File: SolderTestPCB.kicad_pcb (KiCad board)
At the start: 2 copper layers, 2 parts, among them U1 L78L33_TO92, U3 ESP-12F

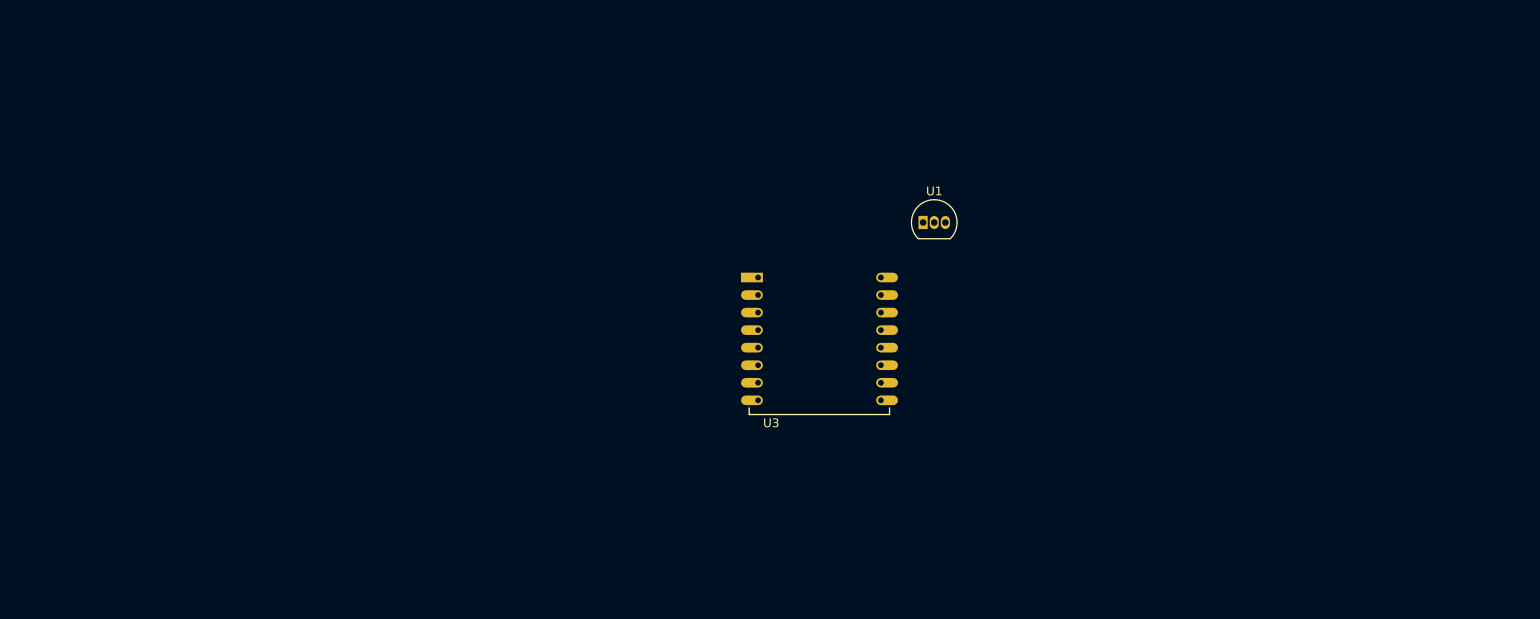
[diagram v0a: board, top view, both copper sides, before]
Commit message: Schematic ready; PCB needs silkscreen
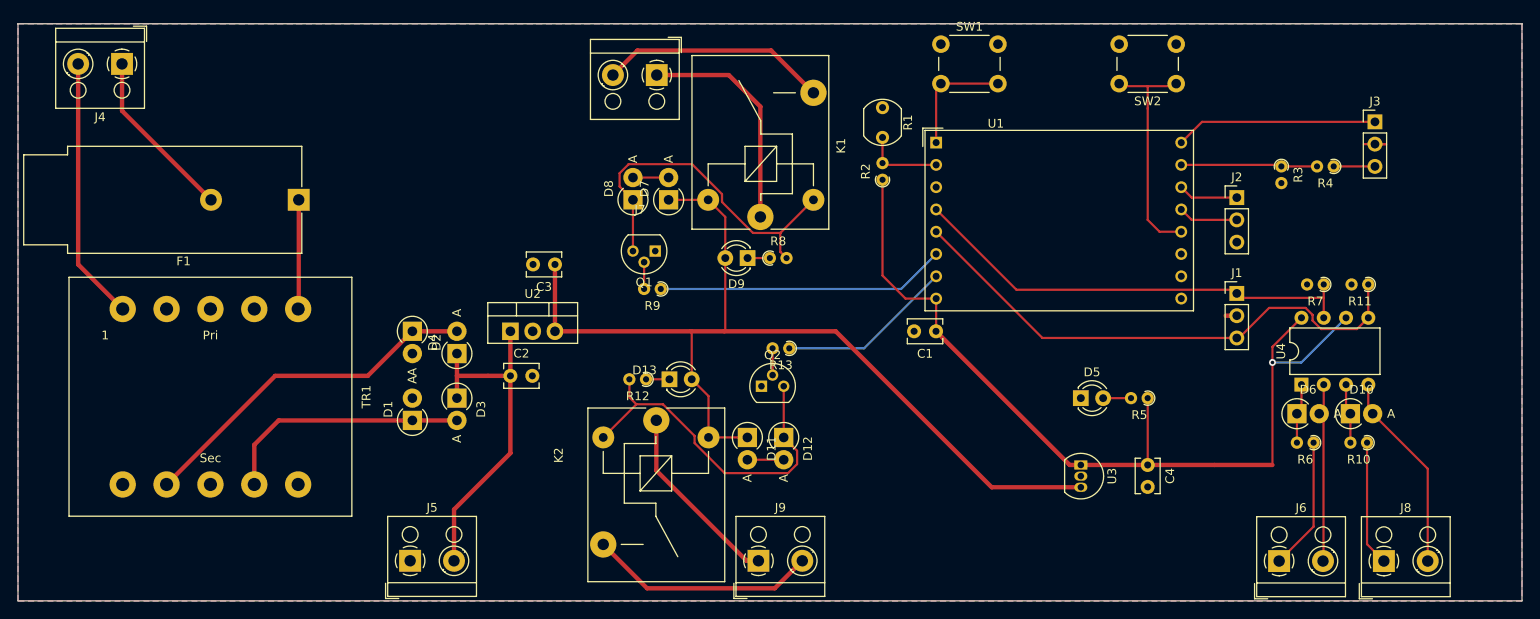
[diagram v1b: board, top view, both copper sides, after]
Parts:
- added C1: 100nF, Capacitor_THT:C_Disc_D3.8mm_W2.6mm_P2.50mm, F.Cu at (170.2, 103.6)
- added C2: C, Capacitor_THT:C_Disc_D3.8mm_W2.6mm_P2.50mm, F.Cu at (121.7, 108.7)
- added C3: C, Capacitor_THT:C_Disc_D3.8mm_W2.6mm_P2.50mm, F.Cu at (126.7, 96.0)
- added C4: C, Capacitor_THT:C_Disc_D3.8mm_W2.6mm_P2.50mm, F.Cu at (194.3, 118.9)
- added D1: D_45deg, Diode_THT:D_DO-41_SOD81_P2.54mm_Vertical_AnodeUp, F.Cu at (110.5, 113.8)
- added D10: D, Diode_THT:D_DO-41_SOD81_P2.54mm_Vertical_AnodeUp, F.Cu at (217.4, 113.0)
- added D11: D, Diode_THT:D_DO-41_SOD81_P2.54mm_Vertical_AnodeUp, F.Cu at (148.7, 115.7)
- added D12: D_Zener, Diode_THT:D_DO-41_SOD81_P2.54mm_Vertical_AnodeUp, F.Cu at (152.8, 115.7)
- added D13: LED, LED_THT:LED_D3.0mm, F.Cu at (139.8, 109.1)
- added D2: D_45deg, Diode_THT:D_DO-41_SOD81_P2.54mm_Vertical_AnodeUp, F.Cu at (110.5, 103.6)
- added D3: D_45deg, Diode_THT:D_DO-41_SOD81_P2.54mm_Vertical_AnodeUp, F.Cu at (115.6, 111.3)
- added D4: D_45deg, Diode_THT:D_DO-41_SOD81_P2.54mm_Vertical_AnodeUp, F.Cu at (115.6, 106.2)
- added D5: LED, LED_THT:LED_D3.0mm, F.Cu at (186.7, 111.3)
- added D6: D, Diode_THT:D_DO-41_SOD81_P2.54mm_Vertical_AnodeUp, F.Cu at (211.3, 113.0)
- added D7: D, Diode_THT:D_DO-41_SOD81_P2.54mm_Vertical_AnodeUp, F.Cu at (139.7, 88.6)
- added D8: D_Zener, Diode_THT:D_DO-41_SOD81_P2.54mm_Vertical_AnodeUp, F.Cu at (135.6, 88.6)
- added D9: LED, LED_THT:LED_D3.0mm, F.Cu at (148.7, 95.3)
- added F1: Fuse, Fuse:Fuseholder_Cylinder-5x20mm_Schurter_FAB_0031-355x_Horizontal_Closed, F.Cu at (97.5, 88.6)
- added J1: CON_INPUT, Connector_PinHeader_2.54mm:PinHeader_1x03_P2.54mm_Vertical, F.Cu at (204.5, 99.3)
- added J2: CON_I2C, Connector_PinHeader_2.54mm:PinHeader_1x03_P2.54mm_Vertical, F.Cu at (204.5, 88.4)
- added J3: CON_SERIAL, Connector_PinHeader_2.54mm:PinHeader_1x03_P2.54mm_Vertical, F.Cu at (220.2, 79.8)
- added J4: Screw_Terminal_01x02, TerminalBlock_RND:TerminalBlock_RND_205-00001_1x02_P5.00mm_Horizontal, F.Cu at (77.4, 73.2)
- added J5: Screw_Terminal_01x02, TerminalBlock_RND:TerminalBlock_RND_205-00001_1x02_P5.00mm_Horizontal, F.Cu at (110.2, 129.8)
- added J6: Screw_Terminal_01x02, TerminalBlock_RND:TerminalBlock_RND_205-00001_1x02_P5.00mm_Horizontal, F.Cu at (209.3, 129.8)
- added J7: Screw_Terminal_01x02, TerminalBlock_RND:TerminalBlock_RND_205-00001_1x02_P5.00mm_Horizontal, F.Cu at (138.3, 74.4)
- added J8: Screw_Terminal_01x02, TerminalBlock_RND:TerminalBlock_RND_205-00001_1x02_P5.00mm_Horizontal, F.Cu at (221.2, 129.8)
- added J9: Screw_Terminal_01x02, TerminalBlock_RND:TerminalBlock_RND_205-00001_1x02_P5.00mm_Horizontal, F.Cu at (149.9, 129.8)
- added K1: Relay_SPST-NO, Relay_THT:Relay_SPST_SANYOU_SRD_Series_Form_A, F.Cu at (150.2, 90.6)
- added K2: Relay_SPST-NO, Relay_THT:Relay_SPST_SANYOU_SRD_Series_Form_A, F.Cu at (138.3, 113.8)
- added Q1: Q_NPN_EBC, Package_TO_SOT_THT:TO-92, F.Cu at (138.2, 94.5)
- added Q2: Q_NPN_EBC, Package_TO_SOT_THT:TO-92, F.Cu at (150.3, 109.9)
- added R1: R_Photo, OptoDevice:R_LDR_5.1x4.3mm_P3.4mm_Vertical, F.Cu at (164.1, 78.1)
- added R10: R, Resistor_THT:R_Axial_DIN0204_L3.6mm_D1.6mm_P1.90mm_Vertical, F.Cu at (219.3, 116.3)
- added R11: R, Resistor_THT:R_Axial_DIN0204_L3.6mm_D1.6mm_P1.90mm_Vertical, F.Cu at (219.5, 98.3)
- added R12: R, Resistor_THT:R_Axial_DIN0204_L3.6mm_D1.6mm_P1.90mm_Vertical, F.Cu at (137.1, 109.1)
- added R13: R, Resistor_THT:R_Axial_DIN0204_L3.6mm_D1.6mm_P1.90mm_Vertical, F.Cu at (153.5, 105.6)
- added R2: R, Resistor_THT:R_Axial_DIN0204_L3.6mm_D1.6mm_P1.90mm_Vertical, F.Cu at (164.1, 86.4)
- added R3: R, Resistor_THT:R_Axial_DIN0204_L3.6mm_D1.6mm_P1.90mm_Vertical, F.Cu at (209.6, 84.8)
- added R4: R, Resistor_THT:R_Axial_DIN0204_L3.6mm_D1.6mm_P1.90mm_Vertical, F.Cu at (215.5, 84.8)
- added R5: R, Resistor_THT:R_Axial_DIN0204_L3.6mm_D1.6mm_P1.90mm_Vertical, F.Cu at (194.3, 111.3)
- added R6: R, Resistor_THT:R_Axial_DIN0204_L3.6mm_D1.6mm_P1.90mm_Vertical, F.Cu at (213.2, 116.3)
- added R7: R, Resistor_THT:R_Axial_DIN0204_L3.6mm_D1.6mm_P1.90mm_Vertical, F.Cu at (214.4, 98.3)
- added R8: R, Resistor_THT:R_Axial_DIN0204_L3.6mm_D1.6mm_P1.90mm_Vertical, F.Cu at (151.2, 95.3)
- added R9: R, Resistor_THT:R_Axial_DIN0204_L3.6mm_D1.6mm_P1.90mm_Vertical, F.Cu at (138.8, 98.8)
- added SW1: SW_RST, Button_Switch_THT:SW_PUSH_6mm_H4.3mm, F.Cu at (170.7, 70.9)
- added SW2: SW_PRG, Button_Switch_THT:SW_PUSH_6mm_H4.3mm, F.Cu at (197.6, 75.4)
- added TR1: TRANSF1, Transformer_THT:Transformer_CHK_EI30-2VA_1xSec, F.Cu at (77.5, 101.1)
- added U2: L7805, Package_TO_SOT_THT:TO-220-3_Vertical, F.Cu at (121.7, 103.6)
- added U4: LTV-827, Package_DIP:DIP-8_W7.62mm, F.Cu at (211.8, 109.7)
- U1: value L78L33_TO92 -> ESP-12; footprint Package_TO_SOT_THT:TO-92_Inline -> RF_Module:HOPERF_RFM9XW_THT
- U3: value ESP-12F -> L78L33_TO92; footprint ESP8266:ESP-12 -> Package_TO_SOT_THT:TO-92_Inline
- moved U3 42.5 mm to (186.7, 118.9), turned to -90 degrees
- moved U1 9.23 mm to (170.2, 82.1)
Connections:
- U1 pad 2: unconnected-(U1-GND-Pad2) -> Net-(U1-ADC)
- U1 pad 3: Net-(U1-VI) -> unconnected-(U1-CH_PD-Pad3)
- U3 pad 1: unconnected-(U3-REST-Pad1) -> VCC
- U3 pad 2: unconnected-(U3-ADC-Pad2) -> GND
- U3 pad 3: unconnected-(U3-CH_PD-Pad3) -> +5V
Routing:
- net +5V: track 0.00 -> 112.6 mm
- net VCC: track 0.00 -> 102.8 mm, vias 0 -> 1
- net Net-(J1-Pin_3): track 0.00 -> 61.4 mm
- net Net-(J1-Pin_1): track 0.00 -> 52.4 mm
- net Net-(D2-K): track 0.00 -> 40.7 mm
- net Net-(D8-K): track 0.00 -> 40.5 mm
- net Net-(D12-K): track 0.00 -> 40.5 mm
- net Net-(D3-K): track 0.00 -> 40.0 mm
- net /Output0/Control: track 0.00 -> 33.1 mm
- net Net-(J4-Pin_2): track 0.00 -> 30.0 mm
- net Net-(D1-K): track 0.00 -> 28.9 mm
- net Net-(U1-GPIO0): track 0.00 -> 26.1 mm
- net Net-(J9-Pin_2): track 0.00 -> 26.1 mm
- net Net-(J7-Pin_2): track 0.00 -> 26.0 mm
- net Net-(J7-Pin_1): track 0.00 -> 25.9 mm
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- added copper zone on B.Cu, net GND
- added copper zone on F.Cu, net GND
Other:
- board outline added: 171.4 x 65.8 mm

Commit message: PCB Layout finished (RTM)
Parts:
- added H1: MountingHole, MountingHole:MountingHole_3.2mm_M3, F.Cu at (70.1, 129.8)
- added H2: MountingHole, MountingHole:MountingHole_3.2mm_M3, F.Cu at (70.1, 73.2)
- added H3: MountingHole, MountingHole:MountingHole_3.2mm_M3, F.Cu at (190.8, 73.2)
- added H4: MountingHole, MountingHole:MountingHole_3.2mm_M3, F.Cu at (190.8, 129.8)
- added H5: MountingHole, MountingHole:MountingHole_2.7mm_M2.5, F.Cu at (80.0, 73.2)
- added H6: MountingHole, MountingHole:MountingHole_2.7mm_M2.5, F.Cu at (104.4, 73.2)
- added H7: MountingHole, MountingHole:MountingHole_2.7mm_M2.5, F.Cu at (80.0, 129.8)
- added H8: MountingHole, MountingHole:MountingHole_2.7mm_M2.5, F.Cu at (104.4, 129.8)
- AC IN: renamed from J4
- C2, C3: footprint Capacitor_THT:C_Disc_D3.8mm_W2.6mm_P2.50mm -> Capacitor_THT:C_Radial_D10.0mm_H12.5mm_P5.00mm
- C4: footprint Capacitor_THT:C_Disc_D3.8mm_W2.6mm_P2.50mm -> Capacitor_THT:C_Radial_D6.3mm_H7.0mm_P2.50mm
- D1, D10, D11, D12, D2, D3, D4, D6, D7, D8: footprint Diode_THT:D_DO-41_SOD81_P2.54mm_Vertical_AnodeUp -> Diode_THT:D_DO-15_P10.16mm_Horizontal
- DC IN: renamed from J5
- Light Sensor: renamed from R1
- moved D6 52.2 mm to (159.5, 119.1)
- moved R6 52.1 mm to (161.5, 122.7)
- moved R11 48.2 mm to (171.7, 105.2)
- moved R7 48.2 mm to (166.6, 105.2)
- moved U4 48.1 mm to (164.1, 115.6)
- moved IN1 47.7 mm to (161.6, 129.8)
- moved IN2 47.7 mm to (173.5, 129.8)
- moved R10 46.3 mm to (173.5, 122.7), turned to 0 degrees
- moved D10 44.6 mm to (173.2, 119.1)
- moved C4 44.0 mm to (153.7, 102.1), turned to 0 degrees
- moved R4 42.0 mm to (176.8, 101.1)
- moved R3 39.6 mm to (174.9, 103.9), turned to 0 degrees
- moved SW_RST 39.0 mm to (180.4, 108.7)
- moved INs 38.6 mm to (165.9, 101.1), turned to 90 degrees
- moved R5 36.2 mm to (158.2, 108.0), turned to -90 degrees
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- renumbered D5 to 3.3V, U1 to ESP8266_ADAPTER, J2 to I2C, J6 to IN1, J8 to IN2, J1 to INs, D9 to OUT1, J7 to OUT1, J9 to OUT2, D13 to OUT2, J3 to SERIAL, SW2 to SW_PRG, SW1 to SW_RST
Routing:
- net VCC: track 102.8 -> 47.0 mm, vias 1 -> 0
- net +5V: track 112.6 -> 61.3 mm
- net Net-(U1-REST): track 13.4 -> 58.6 mm
- net Net-(J1-Pin_3): track 61.4 -> 29.9 mm
- net Net-(D1-K): track 28.9 -> 56.9 mm
- net Net-(J1-Pin_1): track 52.4 -> 27.7 mm
- net Net-(J3-Pin_3): track 4.70 -> 28.4 mm
- net Net-(J3-Pin_1): track 23.1 -> 6.03 mm
- net /Output0/Control: track 33.1 -> 21.0 mm
- net Net-(U1-RXD): track 15.5 -> 26.2 mm
- net Net-(J6-Pin_1): track 15.1 -> 7.12 mm
- net Net-(J8-Pin_1): track 14.3 -> 7.12 mm
- net Net-(D12-K): track 40.5 -> 33.4 mm
- net Net-(D3-K): track 40.0 -> 47.1 mm
- net Net-(D8-K): track 40.5 -> 33.5 mm
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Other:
- board size 171.4 x 65.8 mm -> 129.8 x 65.8 mm
